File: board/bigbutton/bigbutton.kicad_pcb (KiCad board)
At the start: 2 copper layers, 70 x 70 mm, 55 parts, among them J1 SWD, J2 USB_C_Receptacle_USB2.0, SW1 RESET, SW2 SMOL, SW3 LORGE, U1 STM32F302CBTx, U2 ATECC608A-SSHDA, U3 USBLC6-2, U4 SN74LV1T34DBV, U5 MIC5504-3.3YM5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

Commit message: Done with first routing attempt
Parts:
- C14, C15, C16, C17, C18, C19, C5, C6: moved to B.Cu
- moved TP_3V3_1 112.2 mm to (80.0, 119.0)
- moved C6 85.9 mm to (90.0, 88.9)
- moved C5 85.6 mm to (90.0, 87.5)
- moved C14 83.7 mm to (79.4, 100.8)
- moved C13 83.6 mm to (79.5, 81.7)
- moved C21 81.9 mm to (95.4, 110.2), turned to 270 degrees
- moved U2 81.8 mm to (112.0, 91.1)
- moved C7 81.8 mm to (121.0, 82.9), turned to 180 degrees
- moved C20 79.4 mm to (88.2, 107.4)
- moved C15 77.3 mm to (80.9, 129.2)
- moved R1 76.5 mm to (99.0, 86.1), turned to 180 degrees
- moved C12 76.2 mm to (109.8, 76.3), turned to 90 degrees
- moved TP_GND_1 76.1 mm to (80.0, 122.0)
- moved TP_~RST~_1 75.0 mm to (128.8, 86.8)
- moved TP_SCL_1 69.7 mm to (102.9, 94.7)
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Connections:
- net Net-(C7-Pad1) renamed /~RST
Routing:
- net GND: track 16.0 -> 197.9 mm, vias 0 -> 16
- net +3V3: track 25.8 -> 130.2 mm, vias 0 -> 10
- net /~RST: track 0.00 -> 58.9 mm, vias 0 -> 2
- net Net-(SW3-Pad1): track 0.00 -> 51.5 mm, vias 0 -> 4
- net +5V: track 292.4 -> 340.4 mm, vias 2 -> 3
- net Net-(D3-Pad2): track 0.00 -> 34.3 mm, vias 0 -> 2
- net Net-(D2-Pad2): track 0.00 -> 34.2 mm, vias 0 -> 2
- net /I2C_SCL: track 0.00 -> 31.6 mm, vias 0 -> 2
- net /I2C_SDA: track 0.00 -> 30.9 mm, vias 0 -> 2
- net Net-(D4-Pad2): track 0.00 -> 30.3 mm, vias 0 -> 2
- net Net-(D5-Pad2): track 0.00 -> 30.2 mm
- net Net-(SW2-Pad1): track 0.00 -> 30.1 mm, vias 0 -> 1
- net Net-(D7-Pad2): track 0.00 -> 26.8 mm
- net Net-(D6-Pad2): track 0.00 -> 26.8 mm
- net Net-(D1-Pad2): track 0.00 -> 20.4 mm
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- added copper zone on B.Cu, net GND
- added copper zone on F.Cu, net GND
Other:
- board size 70 x 70 mm -> 58 x 64 mm
- net class Default: clearance 0.2 -> 0.127
- rule pad_to_mask_clearance: 0.05 -> 0
- rule trace_clearance: 0.2 -> 0.127
- rule via_min_drill: 0.2 -> 0.3
- rule via_min_size: 0.45 -> 0.6

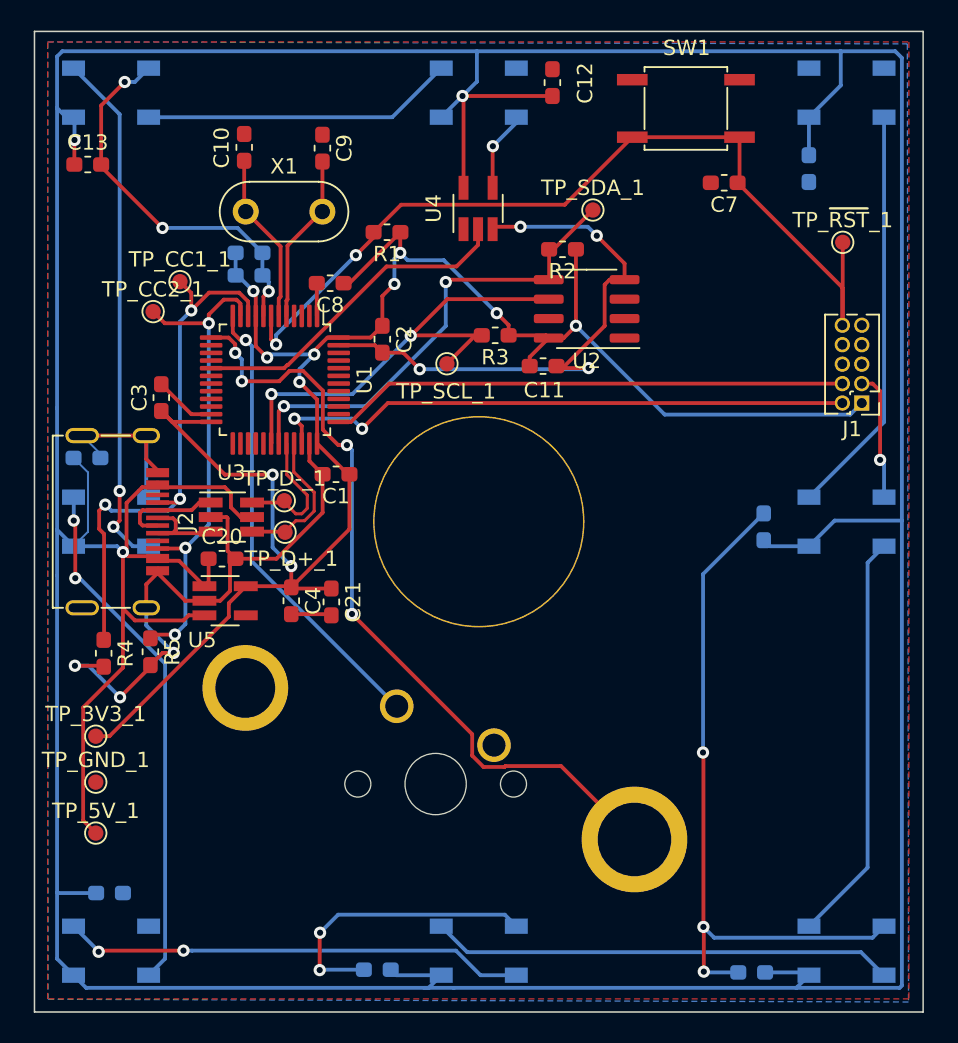
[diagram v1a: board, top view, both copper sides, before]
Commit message: Lots of rerouting
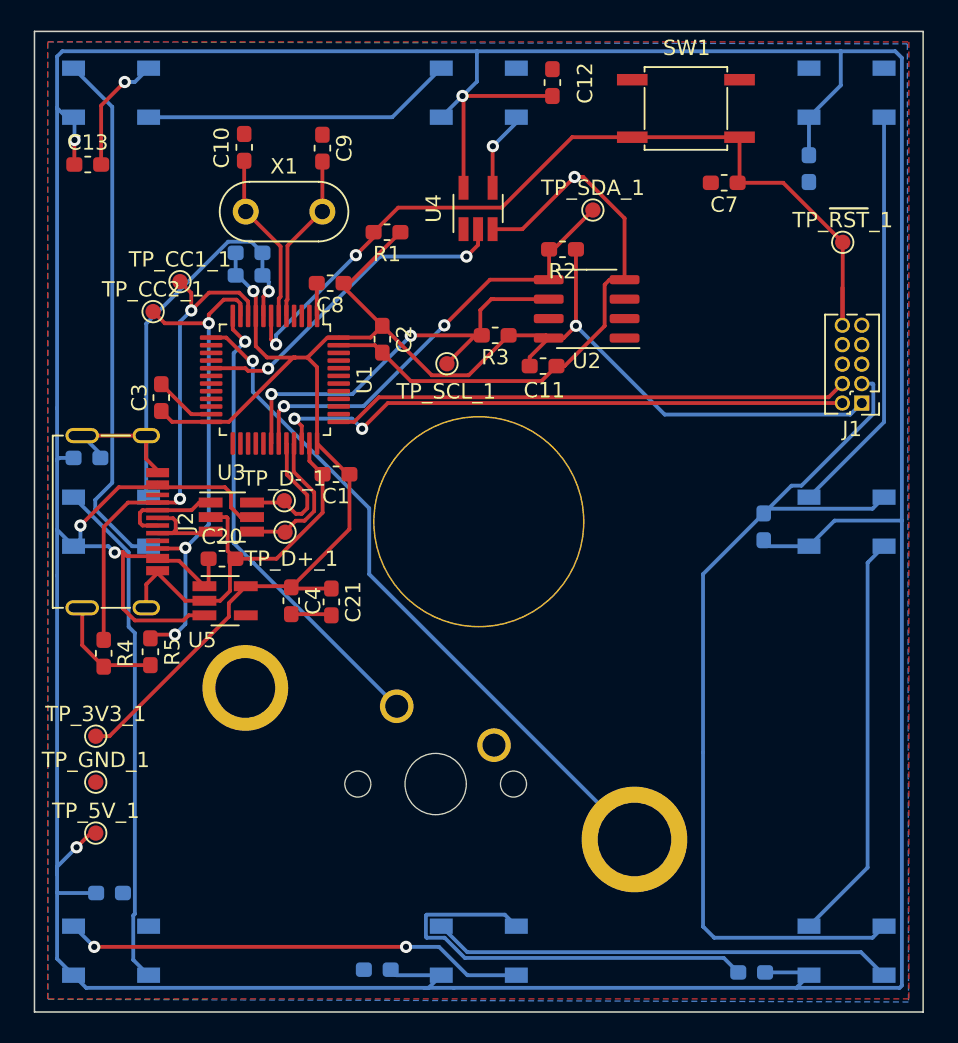
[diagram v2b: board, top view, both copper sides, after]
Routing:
- net GND: track 197.9 -> 213.7 mm, vias 16 -> 3
- net +5V: track 340.4 -> 324.8 mm, vias 3 -> 5
- net +3V3: track 130.2 -> 117.8 mm, vias 10 -> 2
- net Net-(SW3-Pad1): track 51.5 -> 44.9 mm, vias 4 -> 1
- net /I2C_SCL: track 31.6 -> 28.0 mm
- net /USB_CC1: track 36.2 -> 33.3 mm, vias 3 -> 2
- net /I2C_SDA: track 30.9 -> 29.2 mm
- net /~RST: track 58.9 -> 57.8 mm
- net Net-(D3-Pad2): track 34.3 -> 33.3 mm, vias 2 -> 0
- net Net-(D2-Pad2): track 34.2 -> 34.8 mm, vias 2 -> 0
- net Net-(SW2-Pad1): track 30.1 -> 30.7 mm
- net /MCU_DOUT: track 21.8 -> 21.9 mm, vias 0 -> 2

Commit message: Further rerouting
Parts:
- C12, C13, U4: moved to B.Cu
- C5, C6: moved to F.Cu
- moved C6 0.45 mm to (90.2, 89.3)
- moved C5 0.43 mm to (90.2, 87.8)
- turned C12 to 270 degrees
- turned C7 to 0 degrees
- turned U4 to 270 degrees
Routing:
- net +3V3: track 117.8 -> 167.0 mm, vias 2 -> 0
- net GND: track 213.7 -> 250.8 mm, vias 3 -> 2
- net /~RST: track 57.8 -> 89.7 mm, vias 2 -> 1
- net /I2C_SDA: track 29.2 -> 34.1 mm, vias 2 -> 0
- net /USB_CC1: track 33.3 -> 37.3 mm, vias 2 -> 0
- net +5V: track 324.8 -> 321.7 mm, vias 5 -> 2
- net /I2C_SCL: track 28.0 -> 25.1 mm
- net Net-(D1-Pad4): track 5.25 -> 7.95 mm, vias 1 -> 0
- net /MCU_DOUT: track 21.9 -> 24.5 mm, vias 2 -> 1
- net /USB_CC2: track 32.7 -> 35.2 mm, vias 3 -> 2
- net Net-(D2-Pad2): track 34.8 -> 33.2 mm
- net /SWDIO: track 38.6 -> 37.3 mm, vias 2 -> 1
- net Net-(D7-Pad2): track 26.8 -> 27.8 mm
- net Net-(D3-Pad2): track 33.3 -> 34.2 mm
- net /SWCLK: vias 0 -> 1
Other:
- rule trace_min: 0.127 -> 0.25

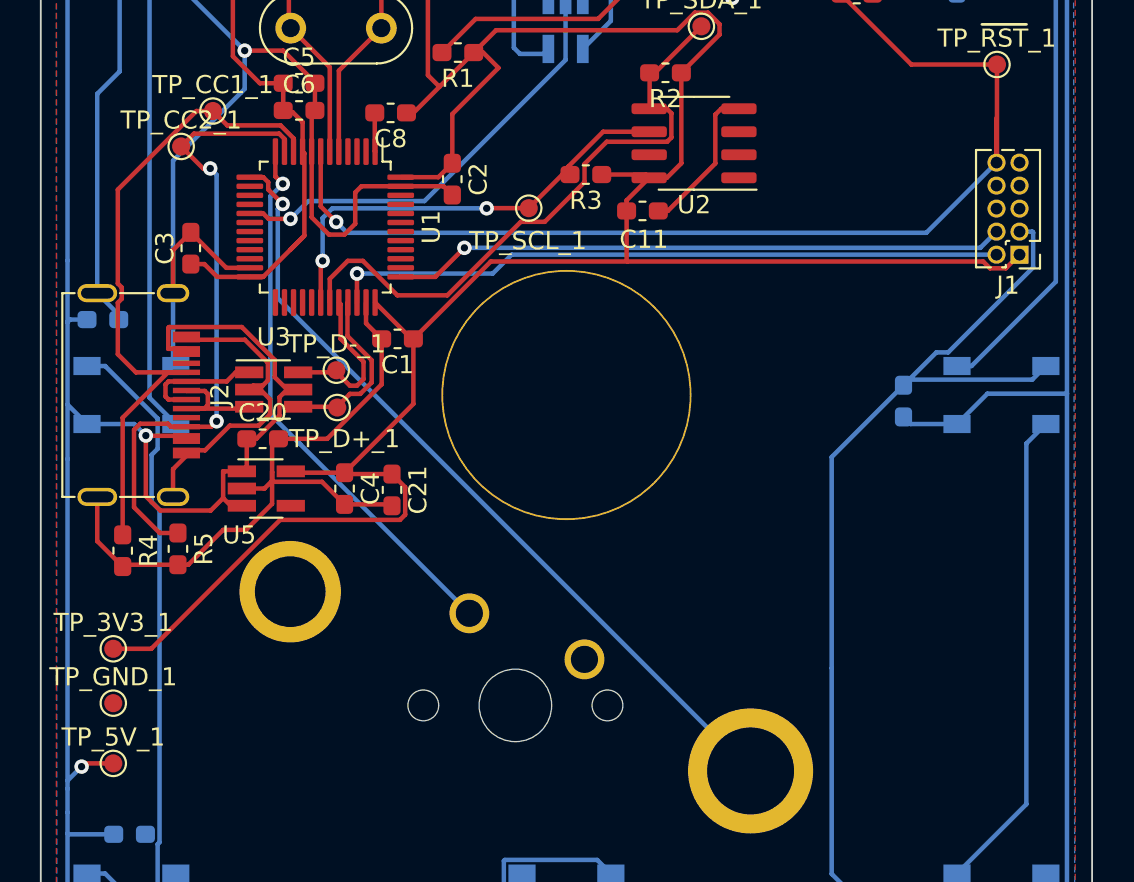
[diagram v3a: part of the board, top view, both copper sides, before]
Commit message: Add BOOT0 button
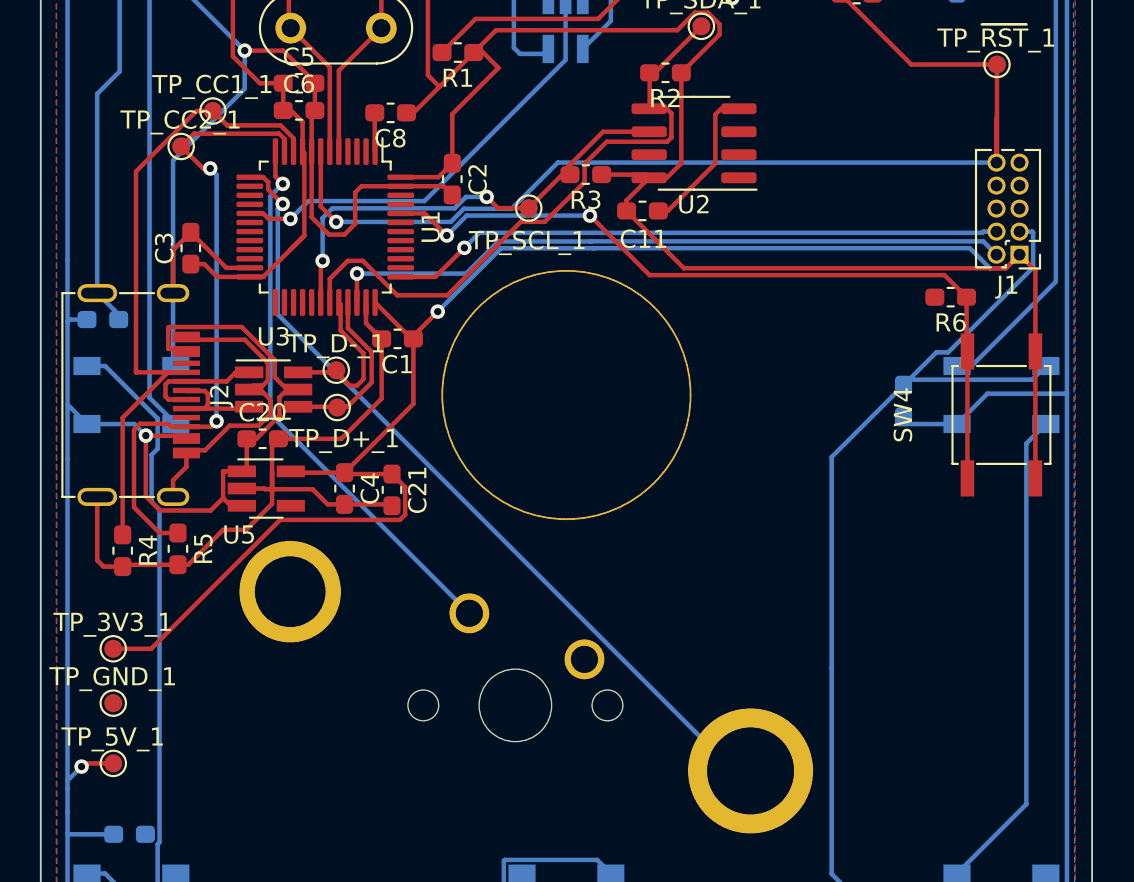
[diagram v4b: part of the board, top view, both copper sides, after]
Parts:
- added R6: 10kΩ, Resistor_SMD:R_0603_1608Metric_Pad1.05x0.95mm_HandSolder, F.Cu at (126.2, 99.6)
- added SW4: BOOT0, bigbutton:SW_SPST_XKB_TS-1187A, F.Cu at (129.0, 106.1)
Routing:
- net /BOOT0: track 0.00 -> 44.1 mm, vias 0 -> 2
- net +3V3: track 167.0 -> 200.9 mm, vias 0 -> 1
- net GND: track 250.8 -> 251.9 mm
- net /USB_CC1: track 37.3 -> 36.3 mm
- net /SWDIO: track 37.3 -> 37.9 mm
- net Net-(SW3-Pad1): track 44.9 -> 45.4 mm
- net /I2C_SCL: track 25.1 -> 25.6 mm

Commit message: Clean up silkscreen
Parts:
- moved TP_SDA_1 10.0 mm to (104.1, 90.2)
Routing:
- net +3V3: track 200.9 -> 190.2 mm
- net /I2C_SDA: track 34.1 -> 36.9 mm

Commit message: Send for production (rev. 1)
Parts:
- renumbered TP_D+_1 to D+, TP_D-_1 to D-
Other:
- board text added: "JLCJLCJLCJLC"
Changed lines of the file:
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@@
   (general
     (thickness 1.6)
-    (drawings 4)
+    (drawings 5)
     (tracks 494)
     (zones 0)
@@
     (0 F.Cu signal)
     (31 B.Cu signal)
-    (32 B.Adhes user)
-    (33 F.Adhes user)
+    (32 B.Adhes user hide)
+    (33 F.Adhes user hide)
     (34 B.Paste user hide)
     (35 F.Paste user hide)
@@
     (visible_elements 7FFFFFFF)
     (pcbplotparams
-      (layerselection 0x010fc_ffffffff)
+      (layerselection 0x010f0_ffffffff)
       (usegerberextensions false)
       (usegerberattributes true)
@@
       (outputformat 1)
       (mirror false)
-      (drillshape 1)
+      (drillshape 0)
       (scaleselection 1)
-      (outputdirectory ""))
+      (outputdirectory "gerber/"))
   )
   (net 0 "")
@@
     (add_net "Net-(U5-Pad4)")
   )
+  (module bigbutton:SW_BIG_SWITCH (layer B.Cu)
+    (at 105 105)
+    (descr "Cherry MX keyswitch, 1.00u, plate mount, http://cherryamericas.com/wp-content/uploads/2014/12/mx_cat.pdf")
+    (tags "Cherry MX keyswitch 1.00u plate")
+    (fp_text reference SW3 (at 0 7.874) (layer B.SilkS)
+      (effects (font (size 1 1) (thickness 0.15)) (justify mirror))
+    )
+    (fp_text value LORGE (at 0 -29) (layer B.Fab)
+      (effects (font (size 1 1) (thickness 0.15)) (justify mirror))
+    )
+    (fp_line (start -27.9 -31.1) (end -27.9 31.1) (layer B.SilkS) (width 0.12))
+    (fp_line (start 27.9 -31.1) (end -27.9 -31.1) (layer B.SilkS) (width 0.12))
+    (fp_line (start 27.9 31.1) (end 27.9 -31.1) (layer B.SilkS) (width 0.12))
+    (fp_line (start -27.9 31.1) (end 27.9 31.1) (layer B.SilkS) (width 0.12))
+    (fp_line (start -6.6 6.6) (end 6.6 6.6) (layer B.CrtYd) (width 0.05))
+    (fp_line (start 6.6 6.6) (end 6.6 -6.6) (layer B.CrtYd) (width 0.05))
+    (fp_line (start 6.6 -6.6) (end -6.6 -6.6) (layer B.CrtYd) (width 0.05))
+    (fp_line (start -6.6 -6.6) (end -6.6 6.6) (layer B.CrtYd) (width 0.05))
+    (fp_line (start -6.35 -6.35) (end -6.35 6.35) (layer B.Fab) (width 0.1))
+    (fp_line (start 6.35 -6.35) (end -6.35 -6.35) (layer B.Fab) (width 0.1))
+    (fp_line (start 6.35 6.35) (end 6.35 -6.35) (layer B.Fab) (width 0.1))
+    (fp_line (start -6.35 6.35) (end 6.35 6.35) (layer B.Fab) (width 0.1))
+    (fp_text user %R (at 0 7.874) (layer B.Fab)
+      (effects (font (size 1 1) (thickness 0.15)) (justify mirror))
+    )
+    (pad "" np_thru_hole circle (at 0 0) (size 13.8 13.8) (drill 13.6) (layers *.Cu *.Mask)
+      (clearance 1))
+    (pad 2 thru_hole circle (at -15.24 10.85) (size 5.6 5.6) (drill 3.9) (layers *.Cu *.Mask)
+      (net 1 GND))
+    (pad 1 thru_hole circle (at 10.16 20.74) (size 6.9 6.9) (drill 4.8) (layers *.Cu *.Mask)
+      (net 49 "Net-(SW3-Pad1)"))
+    (model ${KISYS3DMOD}/Button_Switch_Keyboard.3dshapes/SW_Cherry_MX_1.00u_Plate.wrl
+      (at (xyz 0 0 0))
+      (scale (xyz 1 1 1))
+      (rotate (xyz 0 0 0))
+    )
+  )
   (module bigbutton:SW_SPST_XKB_TS-1187A (layer F.Cu)
     (at 129 106.1 270)
@@
       (net 2 +3V3))
     (model ${KISYS3DMOD}/Connector_PinHeader_1.27mm.3dshapes/PinHeader_2x05_P1.27mm_Vertical.wrl
-      (at (xyz 0 0 0))
-      (scale (xyz 1 1 1))
-      (rotate (xyz 0 0 0))
-    )
-  )
-  (module bigbutton:SW_BIG_SWITCH (layer B.Cu)
-    (at 105 105)
-    (descr "Cherry MX keyswitch, 1.00u, plate mount, http://cherryamericas.com/wp-content/uploads/2014/12/mx_cat.pdf")
-    (tags "Cherry MX keyswitch 1.00u plate")
-    (fp_text reference SW3 (at 0 7.874) (layer B.SilkS)
-      (effects (font (size 1 1) (thickness 0.15)) (justify mirror))
-    )
-    (fp_text value LORGE (at 0 -29) (layer B.Fab)
-      (effects (font (size 1 1) (thickness 0.15)) (justify mirror))
-    )
-    (fp_line (start -27.9 -31.1) (end -27.9 31.1) (layer B.SilkS) (width 0.12))
-    (fp_line (start 27.9 -31.1) (end -27.9 -31.1) (layer B.SilkS) (width 0.12))
-    (fp_line (start 27.9 31.1) (end 27.9 -31.1) (layer B.SilkS) (width 0.12))
-    (fp_line (start -27.9 31.1) (end 27.9 31.1) (layer B.SilkS) (width 0.12))
-    (fp_line (start -6.6 6.6) (end 6.6 6.6) (layer B.CrtYd) (width 0.05))
-    (fp_line (start 6.6 6.6) (end 6.6 -6.6) (layer B.CrtYd) (width 0.05))
-    (fp_line (start 6.6 -6.6) (end -6.6 -6.6) (layer B.CrtYd) (width 0.05))
-    (fp_line (start -6.6 -6.6) (end -6.6 6.6) (layer B.CrtYd) (width 0.05))
-    (fp_line (start -6.35 -6.35) (end -6.35 6.35) (layer B.Fab) (width 0.1))
-    (fp_line (start 6.35 -6.35) (end -6.35 -6.35) (layer B.Fab) (width 0.1))
-    (fp_line (start 6.35 6.35) (end 6.35 -6.35) (layer B.Fab) (width 0.1))
-    (fp_line (start -6.35 6.35) (end 6.35 6.35) (layer B.Fab) (width 0.1))
-    (fp_text user %R (at 0 7.874) (layer B.Fab)
-      (effects (font (size 1 1) (thickness 0.15)) (justify mirror))
-    )
-    (pad "" np_thru_hole circle (at 0 0) (size 13.8 13.8) (drill 13.6) (layers *.Cu *.Mask)
-      (clearance 1))
-    (pad 2 thru_hole circle (at -15.24 10.85) (size 5.6 5.6) (drill 3.9) (layers *.Cu *.Mask)
-      (net 1 GND))
-    (pad 1 thru_hole circle (at 10.16 20.74) (size 6.9 6.9) (drill 4.8) (layers *.Cu *.Mask)
-      (net 49 "Net-(SW3-Pad1)"))
-    (model ${KISYS3DMOD}/Button_Switch_Keyboard.3dshapes/SW_Cherry_MX_1.00u_Plate.wrl
       (at (xyz 0 0 0))
       (scale (xyz 1 1 1))
@@
     (tags "test point SMD pad")
     (attr virtual)
-    (fp_text reference TP_D-_1 (at 0 -1.448) (layer F.SilkS)
+    (fp_text reference D- (at 0 -1.448) (layer F.SilkS)
       (effects (font (size 1 1) (thickness 0.15)))
     )
@@
     (tags "test point SMD pad")
     (attr virtual)
-    (fp_text reference TP_D+_1 (at 3.2456 1.4106) (layer F.SilkS)
+    (fp_text reference D+ (at 2.3456 0.0106) (layer F.SilkS)
       (effects (font (size 1 1) (thickness 0.15)))
     )
@@
     (tags "LED RGB NeoPixel")
     (attr smd)
-    (fp_text reference D5 (at 0 3.5) (layer B.SilkS)
+    (fp_text reference D5 (at 4.7 0) (layer B.SilkS)
       (effects (font (size 1 1) (thickness 0.15)) (justify mirror))
     )
@@
     (tags "LED RGB NeoPixel")
     (attr smd)
-    (fp_text reference D4 (at 0 3.5) (layer B.SilkS)
+    (fp_text reference D4 (at 4.6 0) (layer B.SilkS)
       (effects (font (size 1 1) (thickness 0.15)) (justify mirror))
     )
@@
     (tags "capacitor handsolder")
     (attr smd)
-    (fp_text reference C14 (at 0 1.43) (layer B.SilkS)
+    (fp_text reference C14 (at 3.3742 -0.038) (layer B.SilkS)
       (effects (font (size 1 1) (thickness 0.15)) (justify mirror))
     )
@@
       (rotate (xyz 0 0 0))
     )
+  )
+  (gr_text JLCJLCJLCJLC (at 124.6 131) (layer F.SilkS)
+    (effects (font (size 0.8128 0.8128) (thickness 0.1524)))
   )
   (gr_line (start 76 73) (end 134 73) (layer Edge.Cuts) (width 0.1))
@@
   (segment (start 120.990209 133.473009) (end 104.089837 133.473009) (width 0.25) (layer B.Cu) (net 1))
   (segment (start 121.934 134.4168) (end 120.990209 133.473009) (width 0.25) (layer B.Cu) (net 1))
-  (segment (start 125.407201 102.647999) (end 123.5964 104.4588) (width 0.25) (layer B.Cu) (net 1))
-  (segment (start 126.059403 102.647999) (end 125.407201 102.647999) (width 0.25) (layer B.Cu) (net 1))
-  (segment (start 130.749201 97.958201) (end 126.059403 102.647999) (width 0.25) (layer B.Cu) (net 1))
-  (segment (start 130.749201 96.031495) (end 130.749201 97.958201) (width 0.25) (layer B.Cu) (net 1))
-  (segment (start 130.704306 95.9866) (end 130.749201 96.031495) (width 0.25) (layer B.Cu) (net 1))
-  (segment (start 129.9972 95.9866) (end 130.704306 95.9866) (width 0.25) (layer B.Cu) (net 1))
   (segment (start 123.903199 104.152001) (end 123.5964 104.4588) (width 0.25) (layer B.Cu) (net 1))
   (segment (start 130.697999 104.152001) (end 123.903199 104.152001) (width 0.25) (layer B.Cu) (net 1))
@@
   (segment (start 92.5834 107.4166) (end 94.8068 105.1932) (width 0.25) (layer F.Cu) (net 1))
   (segment (start 88.760799 110.139201) (end 88.760799 109.239201) (width 0.25) (layer F.Cu) (net 1))
-  (segment (start 88.3776 110.2) (end 88.3374 110.1598) (width 0.25) (layer F.Cu) (net 1))
-  (segment (start 91 110.2) (end 88.3776 110.2) (width 0.25) (layer F.Cu) (net 1))
-  (segment (start 92.7608 111.0348) (end 91.8348 111.0348) (width 0.25) (layer F.Cu) (net 1))
-  (segment (start 88.3374 110.1598) (end 87.0928 110.1598) (width 0.25) (layer F.Cu) (net 1))
-  (segment (start 91.8348 111.0348) (end 91 110.2) (width 0.25) (layer F.Cu) (net 1))
   (segment (start 84.0362 108.9638) (end 84.0362 108.35) (width 0.25) (layer F.Cu) (net 1))
   (segment (start 83.2962 110.62) (end 83.2962 109.7038) (width 0.25) (layer F.Cu) (net 1))
@@
   (segment (start 79.1162 114.1162) (end 79.1162 110.62) (width 0.25) (layer F.Cu) (net 1))
   (segment (start 79.4638 114.4638) (end 79.1162 114.1162) (width 0.25) (layer F.Cu) (net 1))
+  (segment (start 88.3374 110.1598) (end 87.0928 110.1598) (width 0.25) (layer F.Cu) (net 1))
+  (segment (start 90.9598 110.1598) (end 88.3374 110.1598) (width 0.25) (layer F.Cu) (net 1))
+  (segment (start 92.7608 111.0348) (end 91.8348 111.0348) (width 0.25) (layer F.Cu) (net 1))
+  (segment (start 91.8348 111.0348) (end 90.9598 110.1598) (width 0.25) (layer F.Cu) (net 1))
+  (segment (start 125.407201 102.647999) (end 123.5964 104.4588) (width 0.25) (layer B.Cu) (net 1))
+  (segment (start 130.046599 98.008601) (end 125.407201 102.647999) (width 0.25) (layer B.Cu) (net 1))
+  (segment (start 130.704306 95.9866) (end 130.749201 96.031495) (width 0.25) (layer B.Cu) (net 1))
+  (segment (start 130.749201 96.031495) (end 130.749201 97.958201) (width 0.25) (layer B.Cu) (net 1))
+  (segment (start 129.9972 95.9866) (end 130.704306 95.9866) (width 0.25) (layer B.Cu) (net 1))
+  (segment (start 130.749201 97.958201) (end 130.698801 98.008601) (width 0.25) (layer B.Cu) (net 1))
+  (segment (start 130.698801 98.008601) (end 130.046599 98.008601) (width 0.25) (layer B.Cu) (net 1))
   (segment (start 96.4537 101.9048) (end 96.5568 101.9048) (width 0.25) (layer F.Cu) (net 2))
   (segment (start 94.444 99.8951) (end 96.4537 101.9048) (width 0.25) (layer F.Cu) (net 2))
